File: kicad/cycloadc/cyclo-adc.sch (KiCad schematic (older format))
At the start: 38 parts

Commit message: various changes to schematics
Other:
- note added: "Add voltage regulator gadget for 2.5v reference!"
- note added: "Maybe do this on cyclo-nexus board."
- note added: "Q: is AREF 2.5v or 5v?"
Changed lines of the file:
@@
 Sheet 1 1
 Title ""
-Date "31 mar 2014"
+Date "5 apr 2014"
 Rev ""
 Comp ""
@@
 	11800 3150 12000 3150
 NoConn ~ 11800 3250
+Text Notes 13200 5050 0    60   ~ 0
+Add voltage regulator gadget for 2.5v reference!
+Text Notes 13200 5350 0    60   ~ 0
+Q: is AREF 2.5v or 5v?
+Text Notes 3200 5350 0    60   ~ 0
+Maybe do this on cyclo-nexus board.
 $EndSCHEMATC

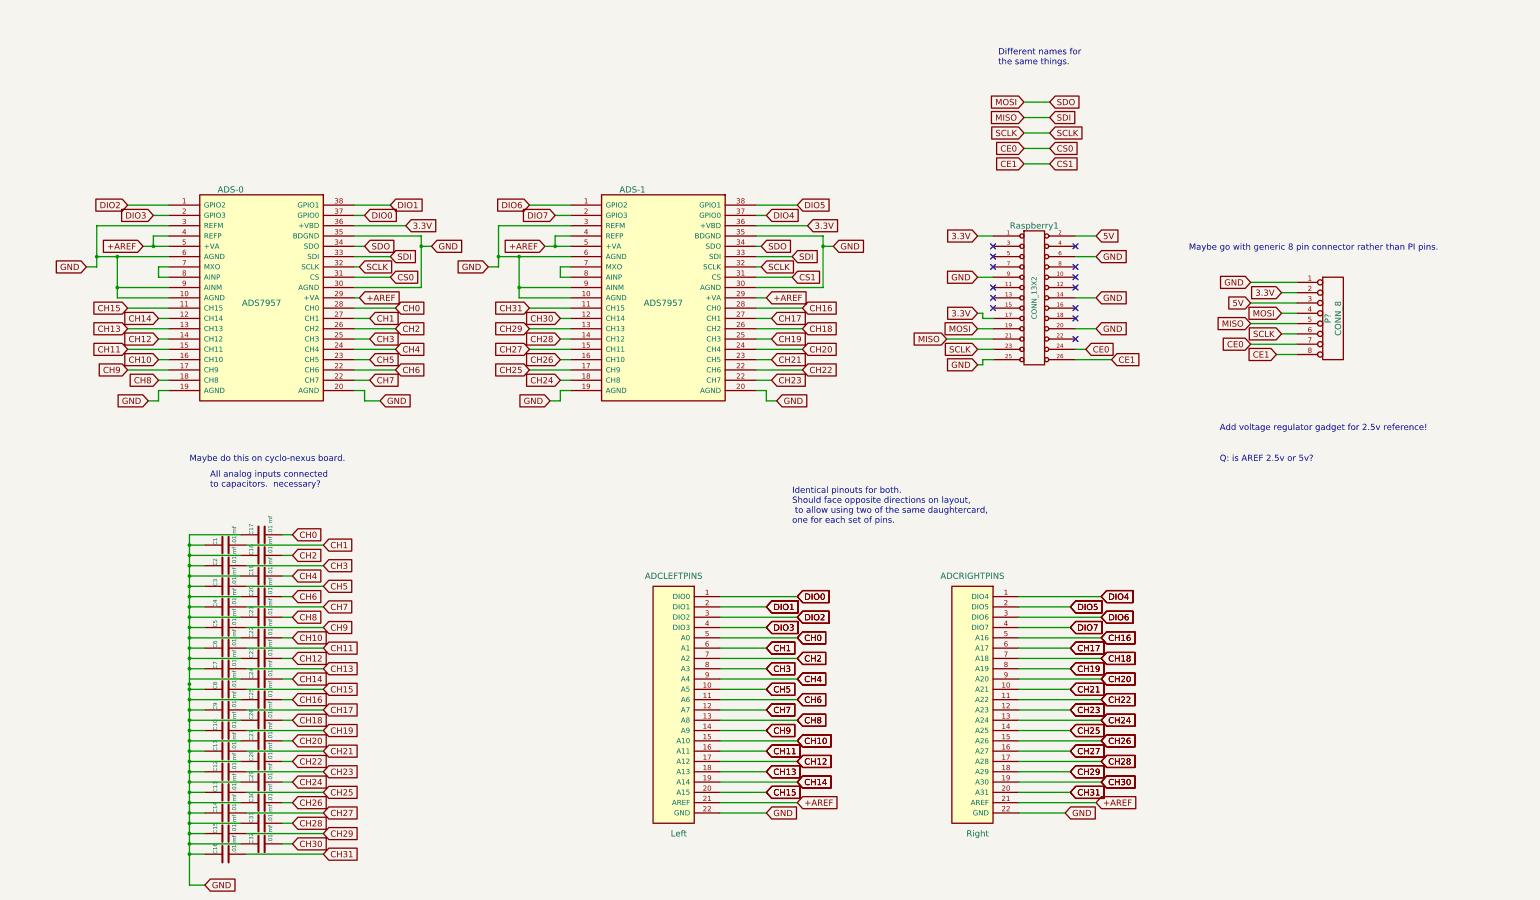
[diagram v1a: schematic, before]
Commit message: add two voltage regulation circuits, the TL431 and LM317 based.  Also update some things - REFP is 2.5v, while AREF is 5v
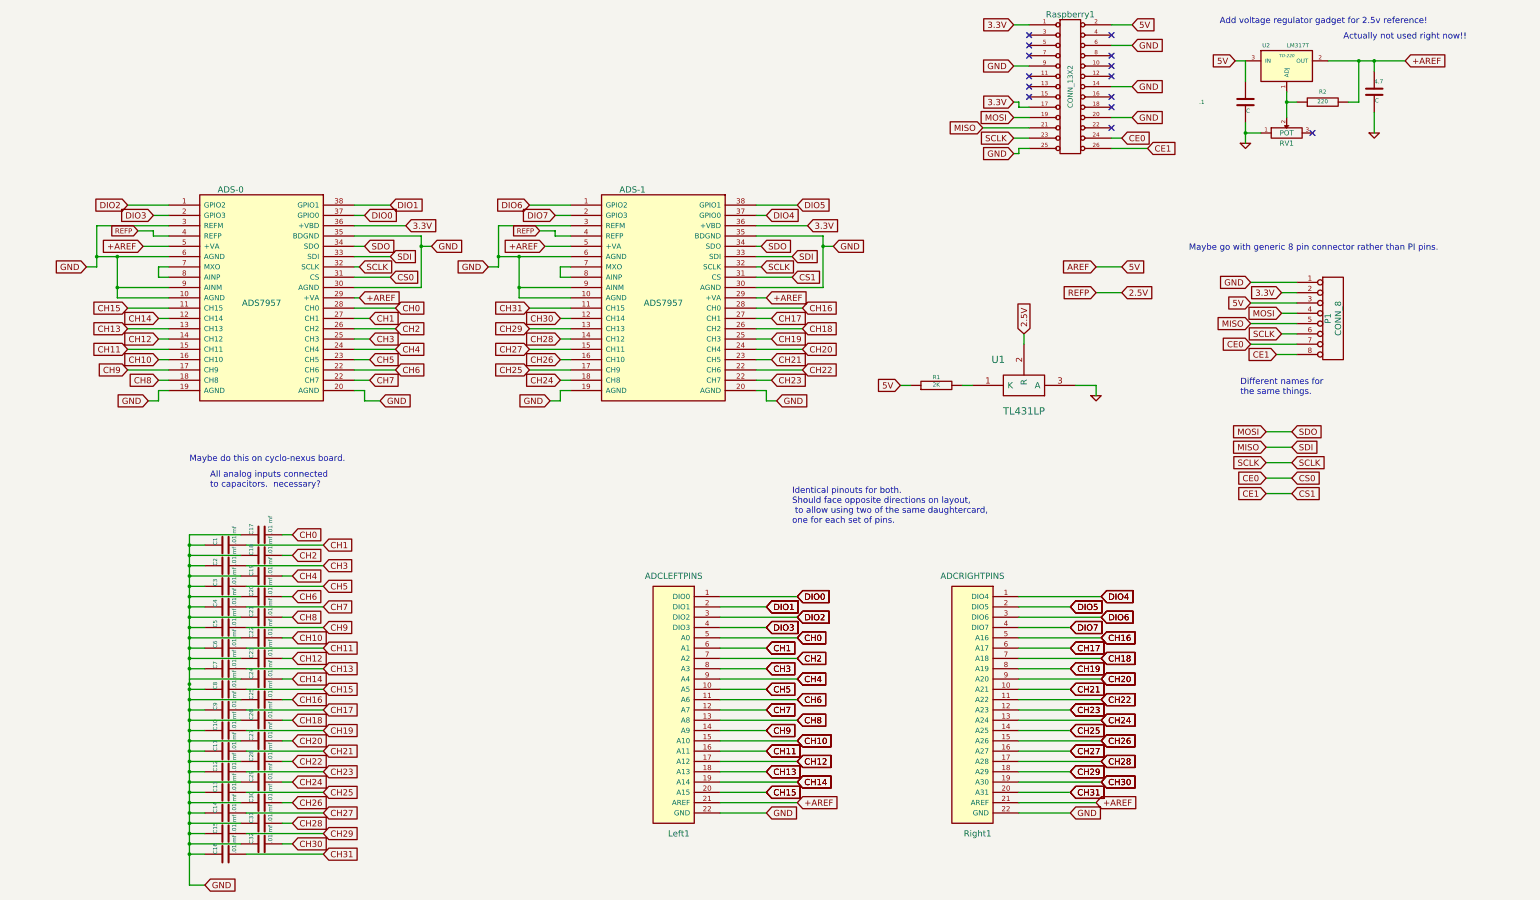
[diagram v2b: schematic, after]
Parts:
- added .1, 4.7: C, ~, symbol C
- added R1: 2K, ~, symbol R
- added R2: 220, ~, symbol R
- added RV1: POT, ~, symbol POT
- added U1: TL431LP, symbol TL431LP
- added U2: LM317T, TO-220, symbol LM317T
- gave numbers to parts that had none: 1
- renumbered Left to Left1, Right to Right1
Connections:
- net +AREF: now also 4.7.1, R2.2, U2.2 (OUT); no longer ADS-0.4 (REFP), ADS-1.4 (REFP)
- net 5V: now also .1.1, R1.1, U2.3 (IN)
- net GND: now also .1.2, 4.7.2, RV1.1, U1.3 (A)
- new net: R2.1, RV1.2, U2.1 (ADJ)
- new net: R1.2, U1.1 (K)
- new net 2.5V: ADS-0.4 (REFP), ADS-1.4 (REFP), U1.2 (R)
- no-connect marks 13 -> 14
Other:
- note added: "Actually not used right now!!"
- note removed: "Q: is AREF 2.5v or 5v?"
- moved on the sheet: Raspberry1

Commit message: various changes!  notes frm Dan.
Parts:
- added C?: C, ~, symbol C
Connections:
- net 2.5V: now also R1.2, U1.1 (K), C?.1
- net GND: now also C?.2
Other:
- note added: "Added re Dan"
- note added: "Bypass Caps for power\n"
- note added: "Change to 3.3?\nMight be ok - then allows \nchange of 5V input"
- note added: "More general purpose: jumper for + and - REFS"
- note added: "bypass cap here? 2.5 to ground"
- note added: "could leave cap empty"
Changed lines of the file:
@@
 Sheet 1 1
 Title ""
-Date "8 apr 2014"
+Date "9 apr 2014"
 Rev ""
 Comp ""
@@
 	11200 1100 11350 1100
 Wire Wire Line
-	5450 3150 5450 3250
-Wire Wire Line
-	5450 3250 5450 3650
+	5450 3150 5450 3650
 Wire Wire Line
 	5450 3650 4800 3650
@@
 Connection ~ 3200 7500
 Wire Wire Line
-	3200 6050 3200 6150
-Wire Wire Line
-	3200 6150 3200 6250
-Wire Wire Line
-	3200 6250 3200 6350
-Wire Wire Line
-	3200 6350 3200 6450
-Wire Wire Line
-	3200 6450 3200 6550
-Wire Wire Line
-	3200 6550 3200 6650
-Wire Wire Line
-	3200 6650 3200 6750
-Wire Wire Line
-	3200 6750 3200 6850
-Wire Wire Line
-	3200 6850 3200 6950
-Wire Wire Line
-	3200 6950 3200 7050
-Wire Wire Line
-	3200 7050 3200 7150
-Wire Wire Line
-	3200 7150 3200 7250
-Wire Wire Line
-	3200 7250 3200 7350
-Wire Wire Line
-	3200 7350 3200 7500
-Wire Wire Line
-	3200 7500 3200 7550
-Wire Wire Line
-	3200 7550 3200 7650
-Wire Wire Line
-	3200 7650 3200 7750
-Wire Wire Line
-	3200 7750 3200 7850
-Wire Wire Line
-	3200 7850 3200 7950
-Wire Wire Line
-	3200 7950 3200 8050
-Wire Wire Line
-	3200 8050 3200 8150
-Wire Wire Line
-	3200 8150 3200 8250
-Wire Wire Line
-	3200 8250 3200 8350
-Wire Wire Line
-	3200 8350 3200 8450
-Wire Wire Line
-	3200 8450 3200 8550
-Wire Wire Line
-	3200 8550 3200 8650
-Wire Wire Line
-	3200 8650 3200 8750
-Wire Wire Line
-	3200 8750 3200 8850
-Wire Wire Line
-	3200 8850 3200 8950
-Wire Wire Line
-	3200 8950 3200 9050
-Wire Wire Line
-	3200 9050 3200 9150
-Wire Wire Line
-	3200 9150 3200 9450
+	3200 6050 3200 9450
 Wire Wire Line
 	3200 7450 3700 7450
@@
 Connection ~ 2500 3650
 Wire Wire Line
-	2500 3350 2500 3650
-Wire Wire Line
-	2500 3650 2500 3750
+	2500 3350 2500 3750
 Wire Wire Line
 	2500 3750 3000 3750
@@
 	4900 4650 4900 4750
 Wire Wire Line
-	2300 3350 2500 3350
-Wire Wire Line
-	2500 3350 3000 3350
+	2300 3350 3000 3350
 Wire Wire Line
 	4800 3750 4850 3750
@@
 	3000 3050 2300 3050
 Wire Wire Line
-	2300 3050 2300 3350
-Wire Wire Line
-	2300 3350 2300 3450
+	2300 3050 2300 3450
 Connection ~ 2300 3350
 Wire Wire Line
@@
 Connection ~ 6200 3350
 Wire Wire Line
-	6200 3050 6200 3350
-Wire Wire Line
-	6200 3350 6200 3450
+	6200 3050 6200 3450
 Wire Wire Line
 	6200 3050 6900 3050
@@
 	8700 3750 8800 3750
 Wire Wire Line
-	6200 3350 6400 3350
-Wire Wire Line
-	6400 3350 6900 3350
+	6200 3350 6900 3350
 Wire Wire Line
 	8800 4650 8800 4750
@@
 	6400 3750 6900 3750
 Wire Wire Line
-	6400 3350 6400 3650
-Wire Wire Line
-	6400 3650 6400 3750
+	6400 3350 6400 3750
 Connection ~ 6400 3650
 Wire Wire Line
@@
 	9350 3650 8700 3650
 Wire Wire Line
-	9350 3150 9350 3250
-Wire Wire Line
-	9350 3250 9350 3650
+	9350 3150 9350 3650
 Wire Wire Line
 	3200 9450 3350 9450
@@
 	14700 1450 14700 1550
 Wire Wire Line
-	14250 1450 14550 1450
-Wire Wire Line
-	14550 1450 14700 1450
-Wire Wire Line
-	14700 1450 15000 1450
-Wire Wire Line
-	13850 1750 13850 1850
-Wire Wire Line
-	13850 1850 13850 2000
+	14250 1450 15000 1450
+Wire Wire Line
+	13850 1750 13850 2000
 Connection ~ 13850 1850
 Wire Wire Line
@@
 	13450 1450 13450 1650
 Wire Wire Line
-	13450 2050 13450 2150
-Wire Wire Line
-	13450 2150 13450 2250
+	13450 2050 13450 2250
 Connection ~ 13450 2150
 Wire Wire Line
@@
 	11300 4100 11300 4200
 Wire Wire Line
-	11800 4600 12000 4600
+	11800 4600 12350 4600
 Wire Wire Line
 	12000 4600 12000 4700
@@
 Wire Wire Line
 	12000 3450 12250 3450
+Text Notes 11700 4150 0    60   ~ 0
+bypass cap here?  2.5 to ground
+Wire Wire Line
+	10800 4200 12350 4200
+Wire Wire Line
+	10800 4600 10800 4200
+Text Notes 10500 4100 0    60   ~ 0
+Added re Dan
+$Comp
+L C C?
+U 1 1 53449C6F
+P 12350 4400
+F 0 "C?" H 12350 4500 40  0000 L CNN
+F 1 "C" H 12356 4315 40  0000 L CNN
+F 2 "~" H 12388 4250 30  0000 C CNN
+F 3 "~" H 12350 4400 60  0000 C CNN
+	1    12350 4400
+	1    0    0    -1
+$EndComp
+Connection ~ 11300 4200
+Connection ~ 12000 4600
+Text Notes 11850 4900 0    60   ~ 0
+could leave cap empty
+Text Notes 6400 5600 0    60   ~ 0
+More general purpose:  jumper for + and - REFS
+Text Notes 13650 2850 0    60   ~ 0
+Bypass Caps for power\n
+Text Notes 9700 4850 0    60   ~ 0
+Change to 3.3?\nMight be ok - then allows \nchange of 5V input
 $EndSCHEMATC

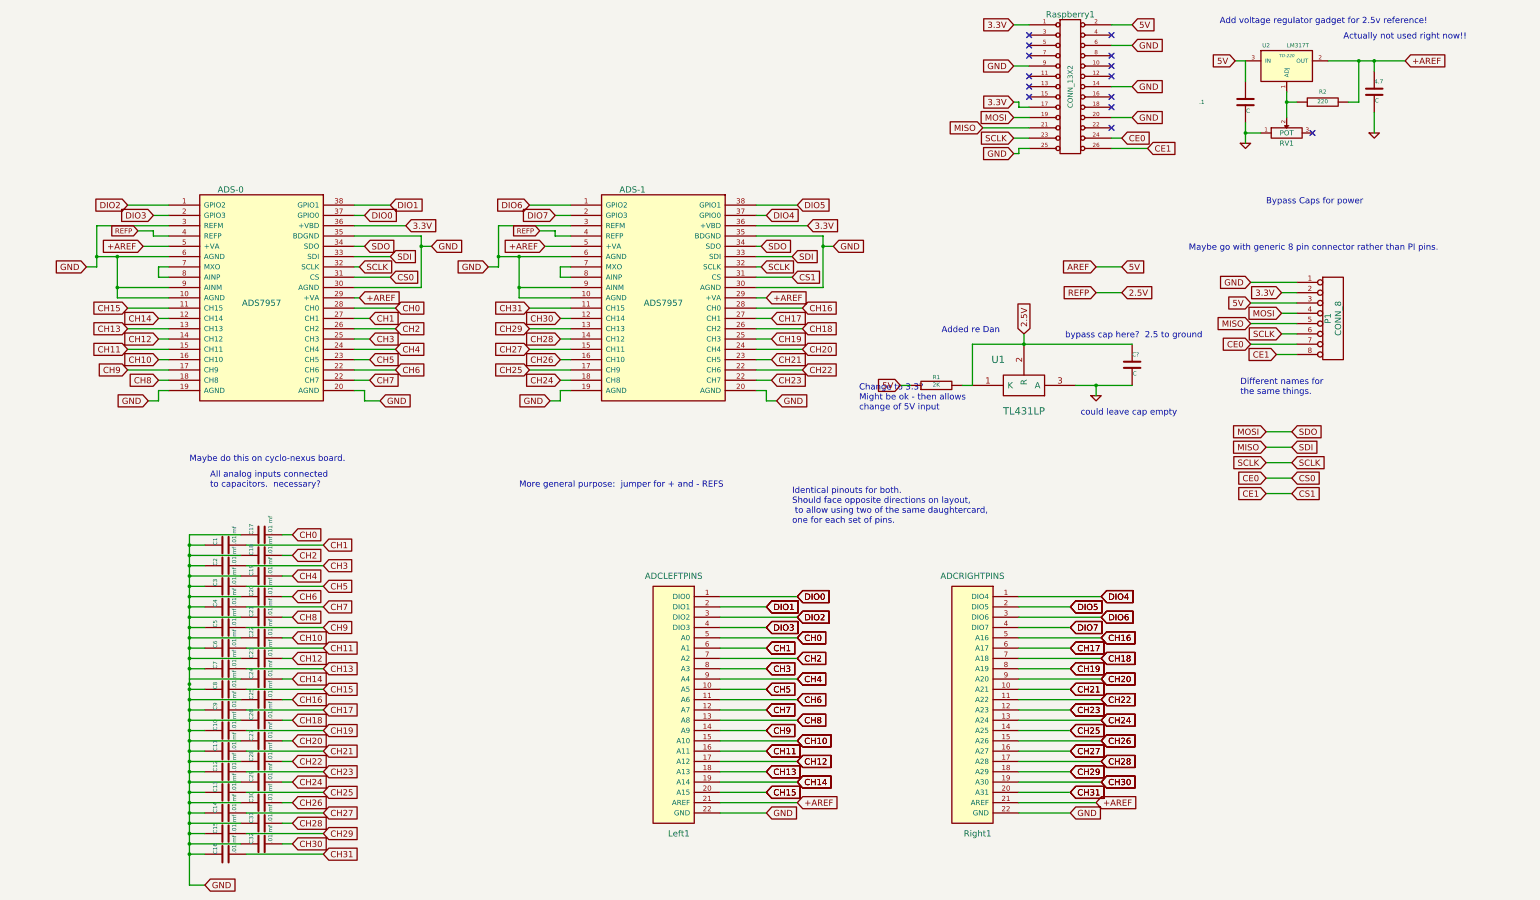
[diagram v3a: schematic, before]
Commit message: remove PI pins, power regulator thingy, add optional DIO connector.
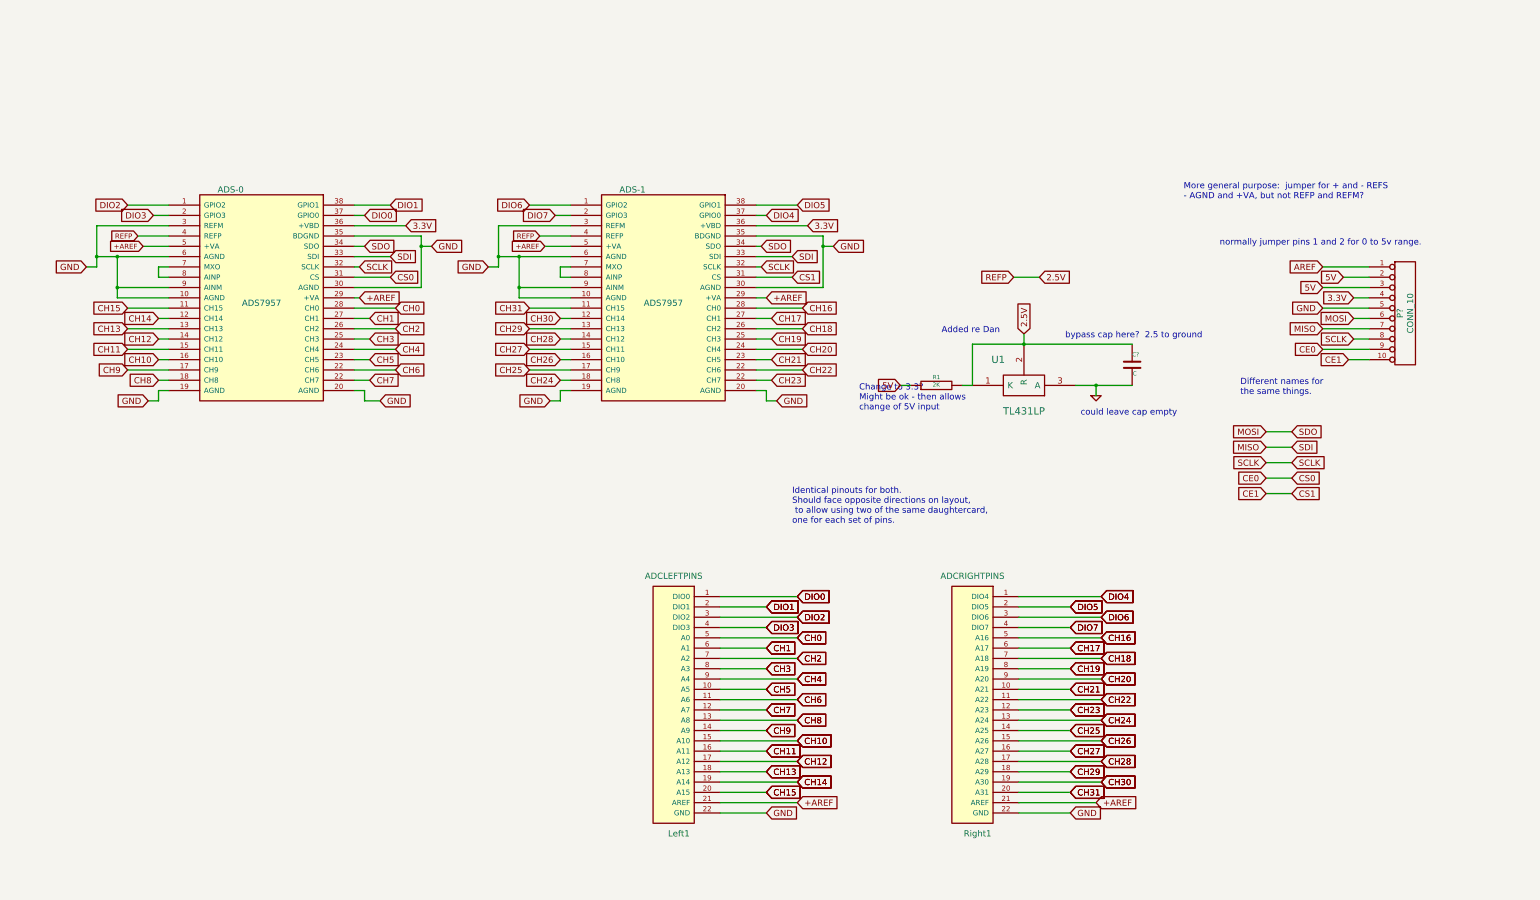
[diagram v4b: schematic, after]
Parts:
- removed .1, 4.7: C, ~, symbol C
- removed C1, C10, C11, C12, C13, C14, C15, C16, C17, C18, C19, C2, C20, C21, C22, C23, C24, C25, C26, C27, C28, C29, C3, C30, C31, C32, C4, C5, C6, C7, C8, C9: .01 mf, ~, symbol C
- removed P1: CONN_8, symbol CONN_8
- removed R2: 220, ~, symbol R
- removed RV1: POT, ~, symbol POT
- removed Raspberry1: CONN_13X2, symbol CONN_13X2
- removed U2: LM317T, TO-220, symbol LM317T
- added P?: CONN_10, symbol CONN_10
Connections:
- net 3.3V: now also P?.4 (P4)
- net 5V: now also P?.2 (P2), P?.3 (P3)
- net CE0: now also P?.9 (P9)
- net CE1: now also P?.10 (P10)
- net GND: now also P?.5 (P5)
- net MISO: now also P?.7 (P7)
- net MOSI: now also P?.6 (P6)
- net SCLK: now also P?.8 (P8)
- new net AREF: P?.1 (P1)
- no-connect marks 14 -> 0
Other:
- note added: "More general purpose: jumper for + and - REFS\n- AGND and +VA, but not REFP and REFM?\n"
- note added: "normally jumper pins 1 and 2 for 0 to 5v range."
- note removed: "Actually not used right now!!"
- note removed: "Add voltage regulator gadget for 2.5v reference!"
- note removed: "All analog inputs connected \nto capacitors. necessary?"
- note removed: "Bypass Caps for power\n"
- note removed: "Maybe do this on cyclo-nexus board."
- note removed: "Maybe go with generic 8 pin connector rather than PI pins.\n"
- note removed: "More general purpose: jumper for + and - REFS"
